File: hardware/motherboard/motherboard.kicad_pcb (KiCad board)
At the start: 4 copper layers, 152 x 68 mm, 85 parts, among them J1 IMU Connector, J2 JST-VH, J3 JST-VH, J4 JST-PH, J5 USB C 2.0, J6 Conn_01x03_Pin, Q1 TSM7P06CP_ROG, Q2 TSM7P06CP_ROG, Q3 AO3400A, Q5 AO3400A, SW1 A, SW10 Right, SW11 Left, SW12 Up, SW13 Reset, SW2 B, SW3 X, SW4 Y, SW5 LB, SW6 RB, SW7 Start, SW8 Select, SW9 Down, U1 ESP32-S3-WROOM-1, U2 MCP73831-2-OT, U3 TPS75533KTTRG3, U4 TLV75709PDBV, U5 COM-09032

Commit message: Updated Motherboard
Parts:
- moved J1 12.0 mm to (96.1, 49.5), turned to -90 degrees
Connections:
- U1 pad 15: unconnected-(U1-IO3-Pad15) -> Status LED
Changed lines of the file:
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@@
 	(net 32 "unconnected-(U1-TXD0-Pad37)")
 	(net 33 "unconnected-(U1-RXD0-Pad36)")
-	(net 34 "unconnected-(U1-IO3-Pad15)")
+	(net 34 "Status LED")
 	(net 35 "ChgStat")
 	(net 36 "AY")
@@
 			(size 1.5 0.9)
 			(layers "F.Cu" "F.Mask" "F.Paste")
-			(net 34 "unconnected-(U1-IO3-Pad15)")
+			(net 34 "Status LED")
 			(pinfunction "IO3")
-			(pintype "bidirectional+no_connect")
+			(pintype "bidirectional")
 		)
 		(pad "16" smd rect
@@
 	(footprint "Connector_PinHeader_2.54mm:PinHeader_1x08_P2.54mm_Vertical"
 		(layer "F.Cu")
-		(at 87.63 57.97 180)
+		(at 96.093657 49.490691 -90)
 		(descr "Through hole straight pin header, 1x08, 2.54mm pitch, single row")
 		(tags "Through hole pin header THT 1x08 2.54mm single row")
 		(property "Reference" "J1"
-			(at 11.775 7.17 0)
+			(at 19.724309 0 90)
 			(layer "F.SilkS")
+			(hide yes)
 			(effects
 				(font
@@
 		)
 		(property "Value" "IMU Connector"
-			(at 0.4425 13.25 0)
+			(at 0.4425 13.25 90)
 			(layer "F.Fab")
 			(effects
@@
 		)
 		(property "Datasheet" "~"
-			(at 0 0 0)
+			(at 0 0 90)
 			(layer "F.Fab")
 			(hide yes)
@@
 		)
 		(property "Description" "Generic connector, single row, 01x08, script generated"
-			(at 0 0 0)
+			(at 0 0 90)
 			(layer "F.Fab")
 			(hide yes)
@@
 		(attr through_hole)
 		(fp_line
-			(start 1.38 1.27)
+			(start -1.38 19.16)
 			(end 1.38 19.16)
 			(stroke
@@
 		)
 		(fp_line
-			(start -1.38 19.16)
-			(end 1.38 19.16)
+			(start -1.38 1.27)
+			(end -1.38 19.16)
 			(stroke
 				(width 0.12)
@@
 		)
 		(fp_line
-			(start -1.38 1.27)
-			(end -1.38 19.16)
+			(start 1.38 1.27)
+			(end 1.38 19.16)
 			(stroke
 				(width 0.12)
@@
 		)
 		(fp_line
-			(start 1.77 19.55)
-			(end 1.77 -1.77)
+			(start -1.77 19.55)
+			(end 1.77 19.55)
 			(stroke
 				(width 0.05)
@@
 		)
 		(fp_line
-			(start 1.77 -1.77)
-			(end -1.77 -1.77)
+			(start 1.77 19.55)
+			(end 1.77 -1.77)
 			(stroke
 				(width 0.05)
@@
 		)
 		(fp_line
-			(start -1.77 19.55)
-			(end 1.77 19.55)
+			(start -1.77 -1.77)
+			(end -1.77 19.55)
 			(stroke
 				(width 0.05)
@@
 		)
 		(fp_line
-			(start -1.77 -1.77)
-			(end -1.77 19.55)
+			(start 1.77 -1.77)
+			(end -1.77 -1.77)
 			(stroke
 				(width 0.05)
@@
 		)
 		(fp_line
-			(start 1.27 19.05)
-			(end -1.27 19.05)
+			(start -1.27 19.05)
+			(end -1.27 -0.635)
 			(stroke
 				(width 0.1)
@@
 		)
 		(fp_line
-			(start 1.27 -1.27)
-			(end 1.27 19.05)
+			(start 1.27 19.05)
+			(end -1.27 19.05)
 			(stroke
 				(width 0.1)
@@
 		)
 		(fp_line
-			(start -0.635 -1.27)
-			(end 1.27 -1.27)
+			(start -1.27 -0.635)
+			(end -0.635 -1.27)
 			(stroke
 				(width 0.1)
@@
 		)
 		(fp_line
-			(start -1.27 19.05)
-			(end -1.27 -0.635)
+			(start -0.635 -1.27)
+			(end 1.27 -1.27)
 			(stroke
 				(width 0.1)
@@
 		)
 		(fp_line
-			(start -1.27 -0.635)
-			(end -0.635 -1.27)
+			(start 1.27 -1.27)
+			(end 1.27 19.05)
 			(stroke
 				(width 0.1)
@@
 		)
 		(fp_text user "${REFERENCE}"
-			(at 0.42 8.47 0)
+			(at 0.42 8.47 90)
 			(layer "F.Fab")
 			(effects
@@
 		)
 		(pad "1" thru_hole rect
-			(at 0 0 180)
+			(at 0 0 270)
 			(size 1.7 1.7)
 			(drill 1)
@@
 		)
 		(pad "2" thru_hole circle
-			(at 0 2.54 180)
+			(at 0 2.54 270)
 			(size 1.7 1.7)
 			(drill 1)
@@
 		)
 		(pad "3" thru_hole circle
-			(at 0 5.08 180)
+			(at 0 5.08 270)
 			(size 1.7 1.7)
 			(drill 1)
@@
 		)
 		(pad "4" thru_hole circle
-			(at 0 7.62 180)
+			(at 0 7.62 270)
 			(size 1.7 1.7)
 			(drill 1)
@@
 		)
 		(pad "5" thru_hole circle
-			(at 0 10.16 180)
+			(at 0 10.16 270)
 			(size 1.7 1.7)
 			(drill 1)
@@
 		)
 		(pad "6" thru_hole circle
-			(at 0 12.7 180)
+			(at 0 12.7 270)
 			(size 1.7 1.7)
 			(drill 1)
@@
 		)
 		(pad "7" thru_hole circle
-			(at 0 15.24 180)
+			(at 0 15.24 270)
 			(size 1.7 1.7)
 			(drill 1)
@@
 		)
 		(pad "8" thru_hole circle
-			(at 0 17.78 180)
+			(at 0 17.78 270)
 			(size 1.7 1.7)
 			(drill 1)
@@
 	)
 	(segment
-		(start 112.285 37.64)
-		(end 112.285 39.48)
+		(start 84.135 40.96)
+		(end 84.135 42.2425)
 		(width 0.5)
 		(layer "F.Cu")
@@
 	)
 	(segment
-		(start 111.125 40.64)
-		(end 84.455 40.64)
+		(start 112.285 37.64)
+		(end 112.285 39.48)
 		(width 0.5)
 		(layer "F.Cu")
@@
 	)
 	(segment
-		(start 84.135 40.96)
-		(end 84.135 42.2425)
+		(start 111.125 40.64)
+		(end 84.455 40.64)
 		(width 0.5)
 		(layer "F.Cu")

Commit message: Routing
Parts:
- removed U5: COM-09032, esp32_handheld:XDCR_COM-09032
- added JY1: ~, esp32_handheld:Adafruit_Joycon, F.Cu at (33.8, 59.5)
- moved R26 11.6 mm to (28.2, 53.2), turned to 180 degrees
- moved C23 4.16 mm to (24.2, 53.2), turned to 0 degrees
- moved C7 1.75 mm to (147.0, 60.0)
- moved C8 1.75 mm to (147.0, 70.8)
- moved R7 1.75 mm to (150.2, 60.0)
- moved R8 1.75 mm to (150.2, 70.8)
- moved SW7 1.75 mm to (137.8, 57.8)
- moved SW8 1.75 mm to (137.8, 68.5)
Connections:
- C23 pad 1: StckBtn -> GND
- C23 pad 2: GND -> StckBtn
- U1 pad 10: Up -> Right
- U1 pad 11: Right -> Up
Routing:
- net Left: track 12.9 -> 135.2 mm, vias 0 -> 1
- net BLeft: track 24.0 -> 135.9 mm, vias 1 -> 3
- net Down: track 13.4 -> 114.0 mm, vias 0 -> 1
- net Up: track 13.6 -> 108.9 mm, vias 0 -> 1
- net Right: track 13.5 -> 95.1 mm, vias 0 -> 1
- net AY: track 118.9 -> 106.9 mm
- net GND: track 235.7 -> 239.8 mm, vias 16 -> 19
- net +3V3: track 36.2 -> 39.6 mm
- net StckBtn: track 110.7 -> 107.8 mm
- net ABat: track 67.0 -> 69.2 mm
- net AX: track 113.8 -> 114.5 mm
- net Start: track 54.3 -> 55.1 mm
- net Select/Boot: track 49.0 -> 49.7 mm
- net ChgStat: track 79.4 -> 80.1 mm

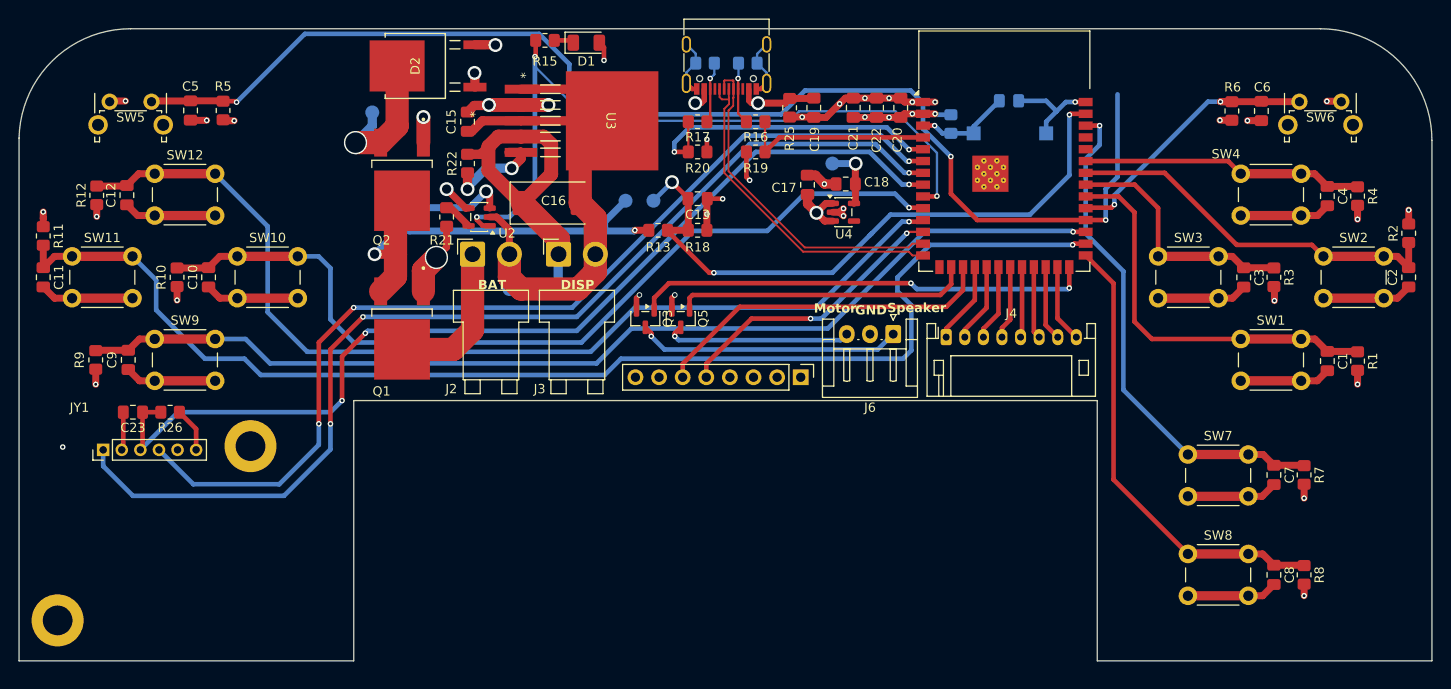
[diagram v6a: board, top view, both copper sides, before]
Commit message: Updated Mounting Holes
Made display holes M3

Matching hole pattern on motherboard to mount display.

Distributed 4, M3 mounting holes throuhout motherboard
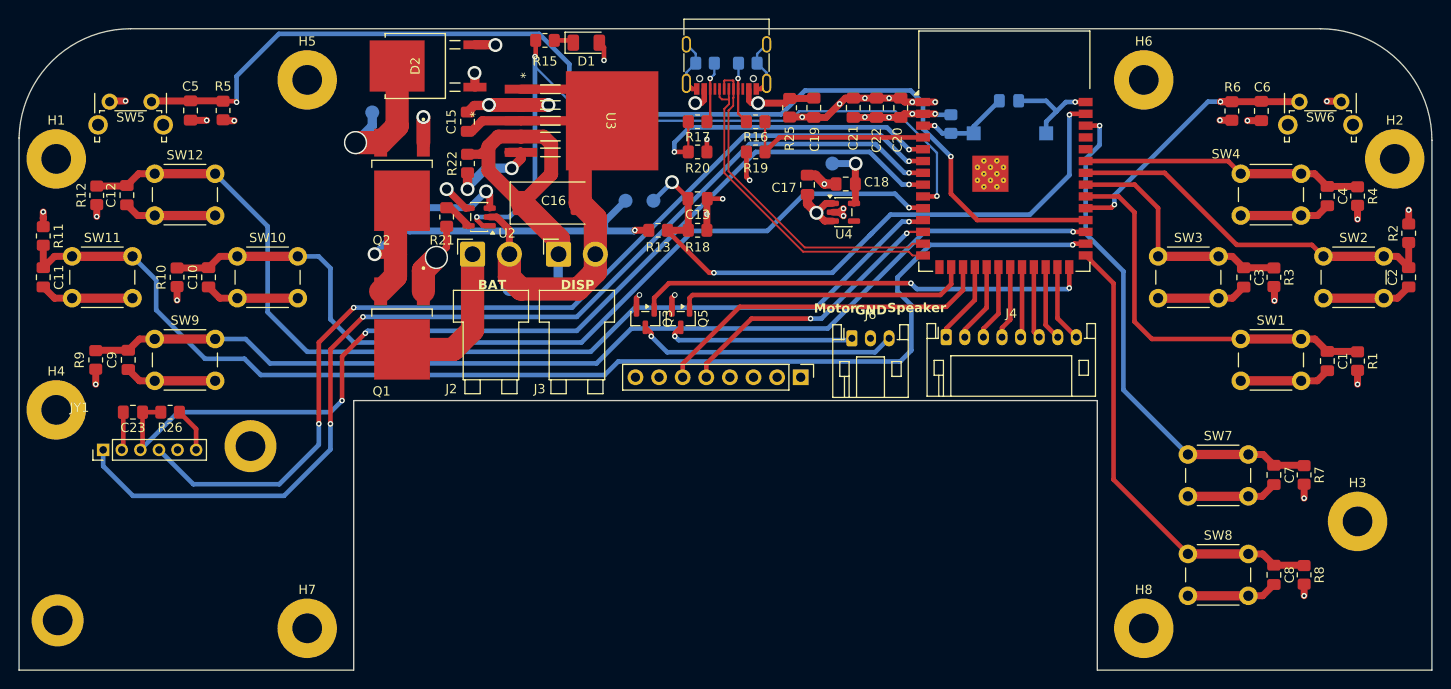
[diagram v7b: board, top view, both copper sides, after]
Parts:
- added H1: MountingHole, MountingHole:MountingHole_3.2mm_M3_Pad, F.Cu at (16.0, 26.0)
- added H2: MountingHole, MountingHole:MountingHole_3.2mm_M3_Pad, F.Cu at (160.0, 26.0)
- added H3: MountingHole, MountingHole:MountingHole_3.2mm_M3_Pad, F.Cu at (156.0, 65.0)
- added H4: MountingHole, MountingHole:MountingHole_3.2mm_M3_Pad, F.Cu at (16.0, 53.0)
- added H5: DisplayMount, MountingHole:MountingHole_3.2mm_M3_Pad, F.Cu at (43.0, 17.5)
- added H6: DisplayMount, MountingHole:MountingHole_3.2mm_M3_Pad, F.Cu at (133.0, 17.5)
- added H7: DisplayMount, MountingHole:MountingHole_3.2mm_M3_Pad, F.Cu at (43.0, 76.5)
- added H8: DisplayMount, MountingHole:MountingHole_3.2mm_M3_Pad, F.Cu at (133.0, 76.5)
- J6: footprint Connector_JST:JST_EH_S3B-EH_1x03_P2.50mm_Horizontal -> Connector_JST:JST_PH_S3B-PH-K_1x03_P2.00mm_Horizontal
- moved J6 4.47 mm to (101.6, 45.3), turned to 0 degrees
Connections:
- Q3 pad 3: Net-(J6-Pin_1) -> Net-(J6-Pin_3)
- Q5 pad 3: Net-(J6-Pin_3) -> Net-(J6-Pin_1)
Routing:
- net BLeft: track 135.9 -> 121.4 mm, vias 3 -> 2
- net Net-(J6-Pin_1): track 28.5 -> 20.5 mm
- net Net-(J6-Pin_3): track 20.2 -> 28.2 mm
- net +3V3: vias 18 -> 17
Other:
- board size 152 x 68 mm -> 152 x 69 mm

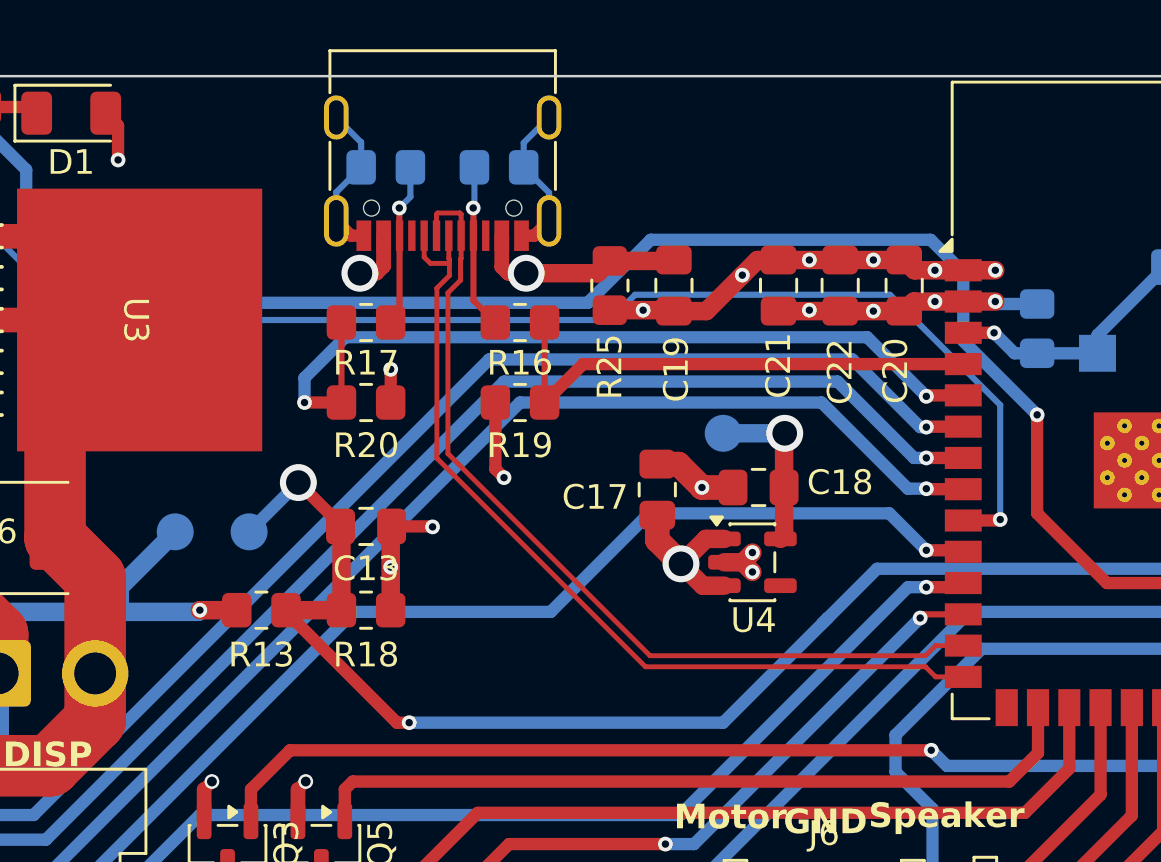
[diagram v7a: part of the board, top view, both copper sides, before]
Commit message: Added status LED trace
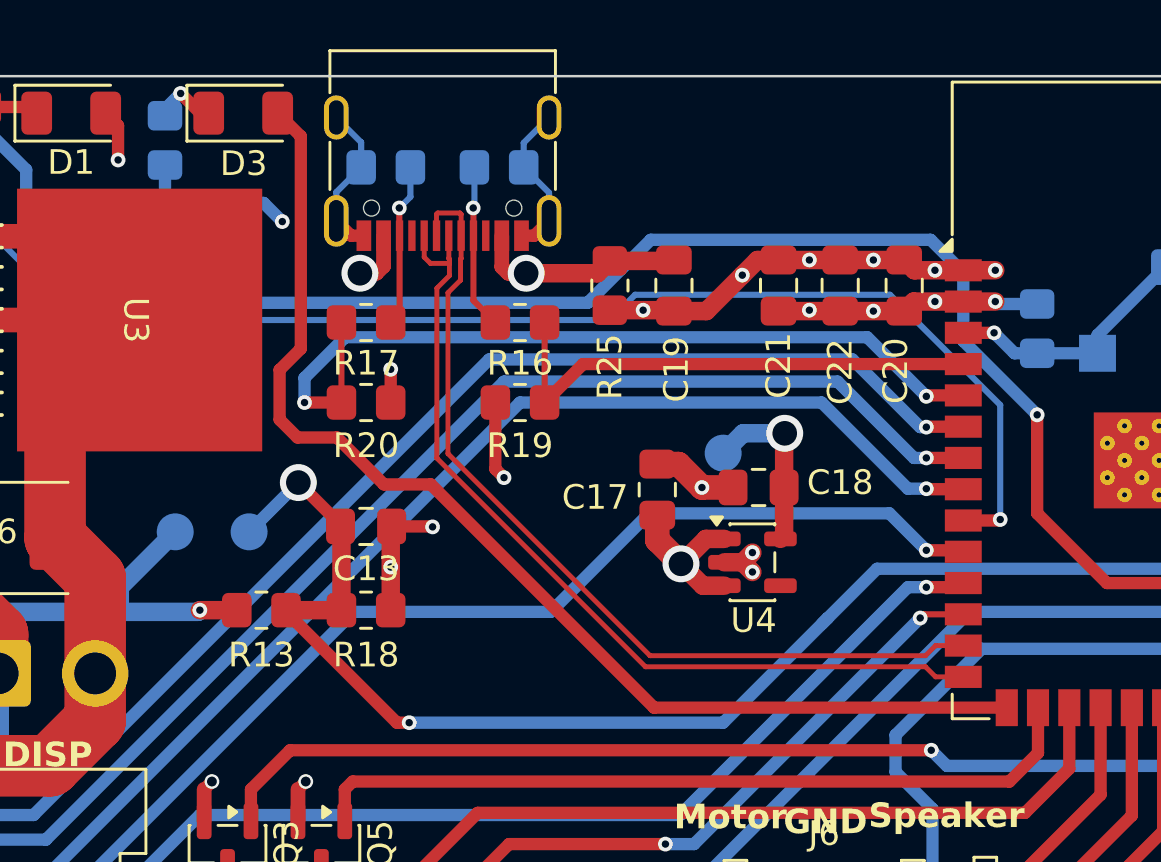
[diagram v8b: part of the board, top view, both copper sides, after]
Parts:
- added D3: StatusLED, LED_SMD:LED_1206_3216Metric, F.Cu at (80.0, 13.5)
- added R27: 100, Resistor_SMD:R_0805_2012Metric_Pad1.20x1.40mm_HandSolder, B.Cu at (76.8, 14.6)
- moved TP6 0.80 mm to (99.5, 27.3)
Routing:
- net Status LED: track 0.00 -> 47.6 mm
- net GND: track 239.8 -> 246.4 mm, vias 19 -> 20
- net Net-(D3-K): track 0.00 -> 2.64 mm, vias 0 -> 1
